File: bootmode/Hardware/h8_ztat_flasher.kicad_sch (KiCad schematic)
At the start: 10 parts, among them J1 Conn_02x05_Counter_Clockwise, Q1 B1187? ~1A or so peak, Q2 NPN?, Q3 PNP? ~300mA or so?

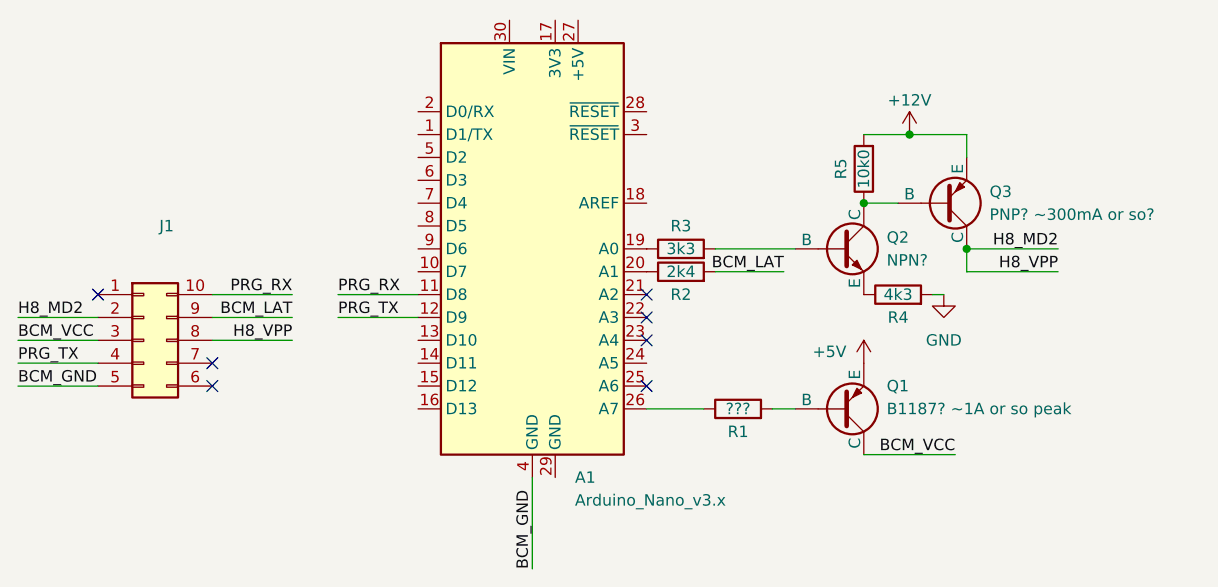
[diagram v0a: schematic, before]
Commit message: feat: flasher: Define R1 to 330 ohms
I need to make sure the 5V rail going to the VCC input of the TA8901SN
combination watchdog and regulator can actually be supplied enough
current.

Back here[^1], I was unable to bring up the VCC pin of the
board. Turns out, by using a 2.7k resistor on the base of the Rohm
B1187 PNP (with a gain value between 60 and 320), I was limiting the
current passed by the transistor and preventing the voltage regulator
from stabilizing.

The math from that post works out, too -- a V_B of 4.1V (compared to
the Arduino output pin) meant that through the 2.7K resistor, only
1.5mA could flow; at hFE=320 (the top of our range), that's at most
480mA of current out to VCC (likely less).

Switching out a 330R resistor "worked". Getting into why:

`V_BE` is limited by saturation on most single-layer BJTs to under 1V,
so (since the emitter is held at 5V), the base current was 4V/330R =
12mA -- even at the bottom of the gain range this translates to 720mA.

I'll likely select another transistor part for my prototype,
since (now that I have a GM328A component tester) I have access to
data on many more parts.

[^1]: https://www.insightcentral.net/threads/dumping-reverse-engineering-insight-g1-bcm-and-mcm-firmare.130914/page-5?post_id=1534367#post-1534367
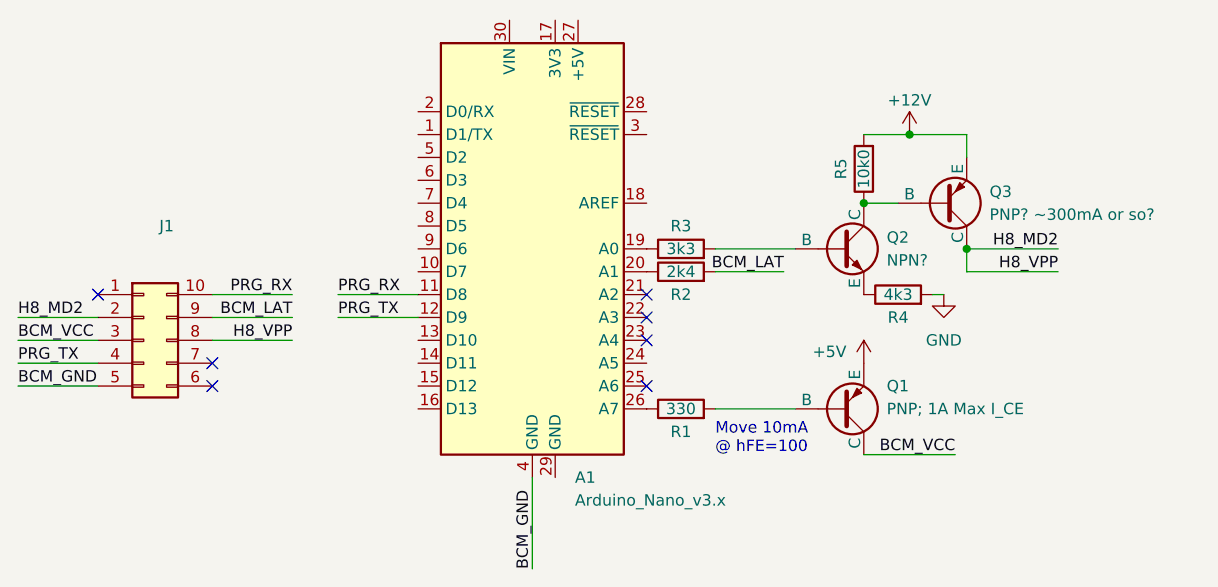
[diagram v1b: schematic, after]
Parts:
- Q1: value B1187? ~1A or so peak -> PNP; 1A Max I_CE
- R1: value ??? -> 330
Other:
- note added: "Move 10mA @ hFE=100"
- moved on the sheet: R1
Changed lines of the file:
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@@
     (stroke (width 0) (type default))
   )
-  (wire (pts (xy 154.94 109.22) (xy 157.48 109.22))
+  (wire (pts (xy 148.59 109.22) (xy 157.48 109.22))
     (stroke (width 0) (type default))
   )
@@
     (stroke (width 0) (type default))
   )
-  (wire (pts (xy 140.97 109.22) (xy 147.32 109.22))
-    (stroke (width 0) (type default))
-  )
   (wire (pts (xy 176.53 91.44) (xy 186.69 91.44))
     (stroke (width 0) (type default))
@@
   (wire (pts (xy 71.12 104.14) (xy 80.01 104.14))
     (stroke (width 0) (type default))
+  )
+  (text "Move 10mA\n@ hFE=100" (at 148.59 114.3 0)
+    (effects (font (size 1.27 1.27)) (justify left bottom))
   )
   (label "H8_MD2" (at 186.69 91.44 180) (fields_autoplaced)
@@
     )
   )
-  (symbol (lib_id "Device:R") (at 151.13 109.22 90) (unit 1)
-    (in_bom yes) (on_board yes) (dnp no)
-    (property "Reference" "R1" (at 151.13 111.76 90)
-      (effects (font (size 1.27 1.27)))
-    )
-    (property "Value" "???" (at 151.13 109.22 90)
-      (effects (font (size 1.27 1.27)))
-    )
-    (property "Footprint" "" (at 151.13 110.998 90)
-      (effects (font (size 1.27 1.27)) hide)
-    )
-    (property "Datasheet" "~" (at 151.13 109.22 0)
+  (symbol (lib_id "Device:R") (at 144.78 109.22 90) (unit 1)
+    (in_bom yes) (on_board yes) (dnp no)
+    (property "Reference" "R1" (at 144.78 111.76 90)
+      (effects (font (size 1.27 1.27)))
+    )
+    (property "Value" "330" (at 144.78 109.22 90)
+      (effects (font (size 1.27 1.27)))
+    )
+    (property "Footprint" "" (at 144.78 110.998 90)
+      (effects (font (size 1.27 1.27)) hide)
+    )
+    (property "Datasheet" "~" (at 144.78 109.22 0)
       (effects (font (size 1.27 1.27)) hide)
     )
@@
       (effects (font (size 1.27 1.27)) (justify left))
     )
-    (property "Value" "B1187? ~1A or so peak" (at 167.64 109.22 0)
-      (effects (font (size 1.27 1.27)) (justify left))
-    )
+    (property "Value" "PNP; 1A Max I_CE" (at 167.64 109.22 0)
+      (effects (font (size 1.27 1.27)) (justify left))
+    )
